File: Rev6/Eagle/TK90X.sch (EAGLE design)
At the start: 217 parts, among them IC1 Z80, IC10 74LS365N, IC11 LM1886, IC12 LM1889, IC13 4116, IC14 4116, IC15 4116, IC16 4116, IC17 4116, IC18 4116, IC19 4116, IC2 ROM, IC20 4116, IC21 4416, IC22 4416, IC23 4416, IC24 4416, IC25 74LS00, IC26 74LS00, IC27 74LS32, IC28 74LS04, IC3 ULA TK90, IC4 74LS74, IC5 74LS74, IC6 74LS157, IC7 74LS157, IC8 74LS157, IC9 74LS157, Q1 BC548, Q2 BC548, Q3 BF494, Q4 BC548, Q5 BD139, Q6 BD136, Q7 BC548, X2 POWER

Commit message: Corrigido conexões power Adicionado jumpers de solda pros jacks de áudio Adicionado revisão 6 com 74LS365 substituido pelo 74LS244
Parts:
- removed C34: 47p, rcl:C-EU050-024X044
- removed C42: 100n, rcl:C-EU050-024X044
- removed D1: 1N4148, tk90:DDO35-12
- removed R52: 22K, rcl:R-EU_0207/5V
- removed R60: ?, rcl:R-EU_0207/5V
- removed VIDEO(RF): RF, testpad:TPPAD1-13
- added C58: 220u, rcl:CPOL-EUE5-6
- added J1, J2: 0R-JUMPB, jump-0r-smd:0R-JUMPB
- added J3, J4: (no value), jumper:SJ
- added Q8: BC517, transistor-npn:BC517
- added R76: 150, rcl:R-EU_0207/5V
- added R77: 75, rcl:R-EU_0207/5V
- added X1: RCA2PINA1, tk90:RCA2PINA1
- C5: value 100n -> 100u; device rcl:C-EU050-024X044 -> rcl:CPOL-EUE5-4
- IC10: value 74LS365N -> 74LS244N; device tk90:74LS365N -> tk90:74LS244N
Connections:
- new net AUDIO: C36.2, C54.2, C55.1, D25_.A, J4.1, R53.1, R54.2
- new net N$33: C26.1, C27.1, IC13.VBB, IC14.VBB, IC15.VBB, IC16.VBB, IC17.VBB, IC18.VBB, IC19.VBB, IC20.VBB, J3.2
- new net N$48: Q8.E, R76.1, R77.1
- new net N$84: IC2.!PGM, J1-0R.2
- new net VDD: C23.1, C25.1, C28.1, C30.1, IC13.VDD, IC14.VDD, IC15.VDD, IC16.VDD, IC17.VDD, IC18.VDD, IC19.VDD, IC20.VDD, J2-0R.2
- net !KBD: now also IC10A.G, IC10B.G; no longer D1.K, IC10A.G1
- net !RD: now also J1-0R.3; no longer IC2.!PGM
- net +12V: now also Q8.C
- net +5V: now also IC10B.A2, IC10B.A4, J1-0R.1, J2-0R.1
- net -5V: now also J3.1; no longer C26.1, C27.1, IC13.VBB, IC14.VBB, IC15.VBB, IC16.VBB, IC17.VBB, IC18.VBB, IC19.VBB, IC20.VBB
- net D4: now also IC10B.Y1; no longer IC10A.Y5
- net D5: now also IC10B.Y2
- net D6: now also IC10B.Y3; no longer IC10A.Y6
- net D7: now also IC10B.Y4; no longer D1.A
- net GND: now also R76.2, X1.2; no longer IC10A.G2, R60.2
- net N$16: now also C5.-; no longer C5.2
- net N$28: now also IC10B.A1; no longer IC10A.A5
- net N$29: now also IC10B.A3; no longer IC10A.A6
- net N$44: no longer MIC.TIP
- net N$50: now also J4.2, MIC.TIP; no longer C36.2, C54.2, C55.1, D25_.A, R53.1, R54.2
- net N$69: now also Q8.B; no longer C34.1
- net N$73: no longer C42.1
- net N$74: now also C58.-, X1.1; no longer C42.2, R60.1, VIDEO(RF).TP
- net N$75: no longer R52.1
- net N$76: now also C58.+, R77.2; no longer C34.2, R52.2
- net N$9: now also C5.+; no longer C5.1
- net V+: now also J2-0R.3; no longer C23.1, C25.1, C28.1, C30.1, IC13.VDD, IC14.VDD, IC15.VDD, IC16.VDD, IC17.VDD, IC18.VDD, IC19.VDD, IC20.VDD, X2.NC
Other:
- note added: "FBLabs rev 6"
- note removed: "FBLabs rev 3"
- moved on the sheet: C26, C27, KB1, MIC, P-1, P-2, P-3, P-4, P-6, R35, R36, R37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

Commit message: Corrigido valor de R49 e outros pequenos detalhes
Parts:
- added J5: (no value), jumper:SJ
- R49: value 1K -> 4K7
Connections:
- new net N$88: EAR.NC, J5.2
- net N$16: now also J5.1; no longer EAR.NC
- net V+: now also X2.NC
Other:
- moved on the sheet: EAR

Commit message: Corrigindo footprint dos jacks RCA Corrigindo lista de peças da revisão 7
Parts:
- X1: value RCA2PINA1 -> RCA2PINN1; device tk90:RCA2PINA1 -> tk90:RCA2PINN1

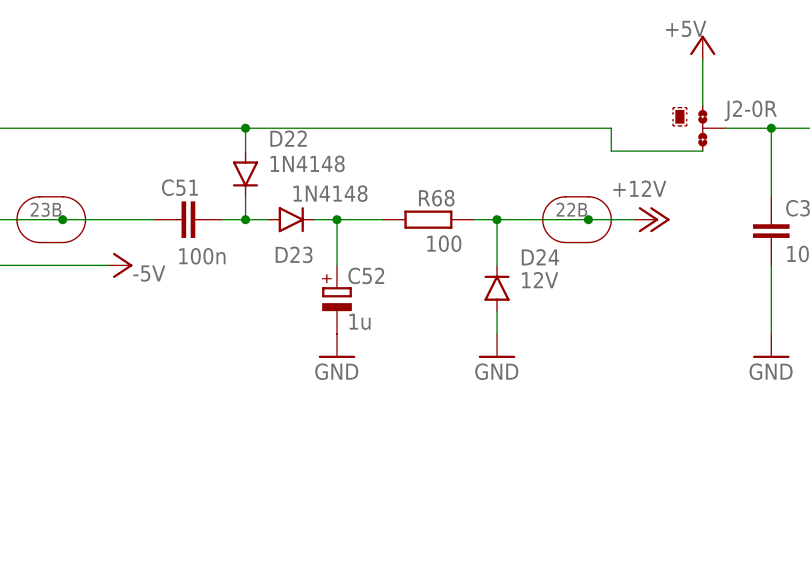
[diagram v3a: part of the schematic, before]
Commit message: Corrigido valores de R68 e C52 para melhor geração dos 12V para o Vídeo e DRAMs. Corrigido largura de algumas trilhas
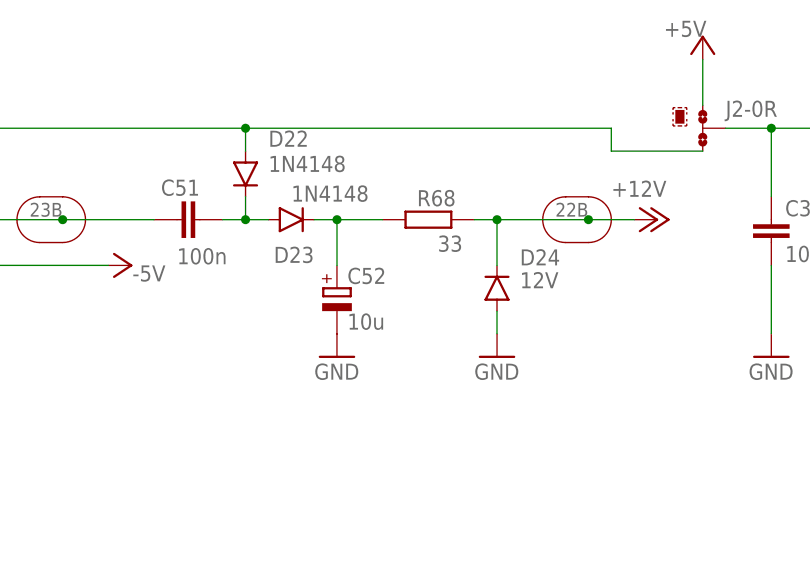
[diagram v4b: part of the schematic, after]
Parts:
- C52: value 1u -> 10u
- R68: value 100 -> 33
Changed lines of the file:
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@@
 <grid distance="0.1" unitdist="inch" unit="inch" style="lines" multiple="1" display="no" altdistance="0.01" altunitdist="inch" altunit="inch"/>
 <layers>
-<layer number="1" name="Top" color="4" fill="1" visible="yes" active="no"/>
-<layer number="2" name="Route2" color="1" fill="3" visible="yes" active="no"/>
-<layer number="3" name="Route3" color="4" fill="3" visible="yes" active="no"/>
-<layer number="4" name="Route4" color="1" fill="4" visible="yes" active="no"/>
-<layer number="5" name="Route5" color="4" fill="4" visible="yes" active="no"/>
-<layer number="6" name="Route6" color="1" fill="8" visible="yes" active="no"/>
-<layer number="7" name="Route7" color="4" fill="8" visible="yes" active="no"/>
-<layer number="8" name="Route8" color="1" fill="2" visible="yes" active="no"/>
-<layer number="9" name="Route9" color="4" fill="2" visible="yes" active="no"/>
-<layer number="10" name="Route10" color="1" fill="7" visible="yes" active="no"/>
-<layer number="11" name="Route11" color="4" fill="7" visible="yes" active="no"/>
-<layer number="12" name="Route12" color="1" fill="5" visible="yes" active="no"/>
-<layer number="13" name="Route13" color="4" fill="5" visible="yes" active="no"/>
-<layer number="14" name="Route14" color="1" fill="6" visible="yes" active="no"/>
-<layer number="15" name="Route15" color="4" fill="6" visible="yes" active="no"/>
-<layer number="16" name="Bottom" color="1" fill="1" visible="yes" active="no"/>
-<layer number="17" name="Pads" color="2" fill="1" visible="yes" active="no"/>
-<layer number="18" name="Vias" color="2" fill="1" visible="yes" active="no"/>
-<layer number="19" name="Unrouted" color="6" fill="1" visible="yes" active="no"/>
-<layer number="20" name="Dimension" color="15" fill="1" visible="yes" active="no"/>
-<layer number="21" name="tPlace" color="7" fill="1" visible="yes" active="no"/>
-<layer number="22" name="bPlace" color="7" fill="1" visible="yes" active="no"/>
-<layer number="23" name="tOrigins" color="15" fill="1" visible="yes" active="no"/>
-<layer number="24" name="bOrigins" color="15" fill="1" visible="yes" active="no"/>
-<layer number="25" name="tNames" color="7" fill="1" visible="yes" active="no"/>
-<layer number="26" name="bNames" color="7" fill="1" visible="yes" active="no"/>
-<layer number="27" name="tValues" color="9" fill="1" visible="yes" active="no"/>
-<layer number="28" name="bValues" color="7" fill="1" visible="yes" active="no"/>
+<layer number="1" name="Top" color="4" fill="1" visible="no" active="no"/>
+<layer number="2" name="Route2" color="1" fill="3" visible="no" active="no"/>
+<layer number="3" name="Route3" color="4" fill="3" visible="no" active="no"/>
+<layer number="4" name="Route4" color="1" fill="4" visible="no" active="no"/>
+<layer number="5" name="Route5" color="4" fill="4" visible="no" active="no"/>
+<layer number="6" name="Route6" color="1" fill="8" visible="no" active="no"/>
+<layer number="7" name="Route7" color="4" fill="8" visible="no" active="no"/>
+<layer number="8" name="Route8" color="1" fill="2" visible="no" active="no"/>
+<layer number="9" name="Route9" color="4" fill="2" visible="no" active="no"/>
+<layer number="10" name="Route10" color="1" fill="7" visible="no" active="no"/>
+<layer number="11" name="Route11" color="4" fill="7" visible="no" active="no"/>
+<layer number="12" name="Route12" color="1" fill="5" visible="no" active="no"/>
+<layer number="13" name="Route13" color="4" fill="5" visible="no" active="no"/>
+<layer number="14" name="Route14" color="1" fill="6" visible="no" active="no"/>
+<layer number="15" name="Route15" color="4" fill="6" visible="no" active="no"/>
+<layer number="16" name="Bottom" color="1" fill="1" visible="no" active="no"/>
+<layer number="17" name="Pads" color="2" fill="1" visible="no" active="no"/>
+<layer number="18" name="Vias" color="2" fill="1" visible="no" active="no"/>
+<layer number="19" name="Unrouted" color="6" fill="1" visible="no" active="no"/>
+<layer number="20" name="Dimension" color="15" fill="1" visible="no" active="no"/>
+<layer number="21" name="tPlace" color="7" fill="1" visible="no" active="no"/>
+<layer number="22" name="bPlace" color="7" fill="1" visible="no" active="no"/>
+<layer number="23" name="tOrigins" color="15" fill="1" visible="no" active="no"/>
+<layer number="24" name="bOrigins" color="15" fill="1" visible="no" active="no"/>
+<layer number="25" name="tNames" color="7" fill="1" visible="no" active="no"/>
+<layer number="26" name="bNames" color="7" fill="1" visible="no" active="no"/>
+<layer number="27" name="tValues" color="9" fill="1" visible="no" active="no"/>
+<layer number="28" name="bValues" color="7" fill="1" visible="no" active="no"/>
 <layer number="29" name="tStop" color="7" fill="3" visible="no" active="no"/>
 <layer number="30" name="bStop" color="7" fill="6" visible="no" active="no"/>
@@
 <layer number="35" name="tGlue" color="7" fill="4" visible="no" active="no"/>
 <layer number="36" name="bGlue" color="7" fill="5" visible="no" active="no"/>
-<layer number="37" name="tTest" color="7" fill="1" visible="yes" active="no"/>
-<layer number="38" name="bTest" color="7" fill="1" visible="yes" active="no"/>
+<layer number="37" name="tTest" color="7" fill="1" visible="no" active="no"/>
+<layer number="38" name="bTest" color="7" fill="1" visible="no" active="no"/>
 <layer number="39" name="tKeepout" color="4" fill="11" visible="no" active="no"/>
 <layer number="40" name="bKeepout" color="1" fill="11" visible="no" active="no"/>
@@
 <layer number="44" name="Drills" color="7" fill="1" visible="no" active="no"/>
 <layer number="45" name="Holes" color="7" fill="1" visible="no" active="no"/>
-<layer number="46" name="Milling" color="3" fill="1" visible="yes" active="no"/>
-<layer number="47" name="Measures" color="7" fill="1" visible="yes" active="no"/>
-<layer number="48" name="Document" color="7" fill="1" visible="yes" active="no"/>
-<layer number="49" name="Reference" color="7" fill="1" visible="yes" active="no"/>
-<layer number="50" name="dxf" color="7" fill="1" visible="yes" active="no"/>
-<layer number="51" name="tDocu" color="7" fill="1" visible="yes" active="no"/>
-<layer number="52" name="bDocu" color="7" fill="1" visible="yes" active="no"/>
-<layer number="53" name="tGND_GNDA" color="7" fill="9" visible="yes" active="no"/>
-<layer number="54" name="bGND_GNDA" color="1" fill="9" visible="yes" active="no"/>
-<layer number="56" name="wert" color="7" fill="1" visible="yes" active="no"/>
+<layer number="46" name="Milling" color="3" fill="1" visible="no" active="no"/>
+<layer number="47" name="Measures" color="7" fill="1" visible="no" active="no"/>
+<layer number="48" name="Document" color="7" fill="1" visible="no" active="no"/>
+<layer number="49" name="Reference" color="7" fill="1" visible="no" active="no"/>
+<layer number="50" name="dxf" color="7" fill="1" visible="no" active="no"/>
+<layer number="51" name="tDocu" color="7" fill="1" visible="no" active="no"/>
+<layer number="52" name="bDocu" color="7" fill="1" visible="no" active="no"/>
+<layer number="53" name="tGND_GNDA" color="7" fill="9" visible="no" active="no"/>
+<layer number="54" name="bGND_GNDA" color="1" fill="9" visible="no" active="no"/>
+<layer number="56" name="wert" color="7" fill="1" visible="no" active="no"/>
 <layer number="90" name="Modules" color="5" fill="1" visible="yes" active="yes"/>
 <layer number="91" name="Nets" color="2" fill="1" visible="yes" active="yes"/>
@@
 <part name="GND41" library="supply1" deviceset="GND" device=""/>
 <part name="P-2" library="supply1" deviceset="-5V" device=""/>
-<part name="C52" library="rcl" deviceset="CPOL-EU" device="E2-5" value="1u"/>
+<part name="C52" library="rcl" deviceset="CPOL-EU" device="E2-5" value="10u"/>
 <part name="C51" library="rcl" deviceset="C-EU" device="050-024X044" value="100n"/>
-<part name="R68" library="rcl" deviceset="R-EU_" device="0207/12" value="100"/>
+<part name="R68" library="rcl" deviceset="R-EU_" device="0207/12" value="33"/>
 <part name="GND42" library="supply1" deviceset="GND" device=""/>
 <part name="GND43" library="supply1" deviceset="GND" device=""/>
